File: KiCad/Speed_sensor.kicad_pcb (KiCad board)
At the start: 4 copper layers, 35 x 20 mm, 65 parts, among them J1 USB_B_Micro, J2 SWD, U1 BQ24040DSQR, U2 TP1941U, U3 ST1PS02, U4 nRF52832-QFxx, U5 LIS2DH12, Y1 32,768kHz, Y2 32MHz

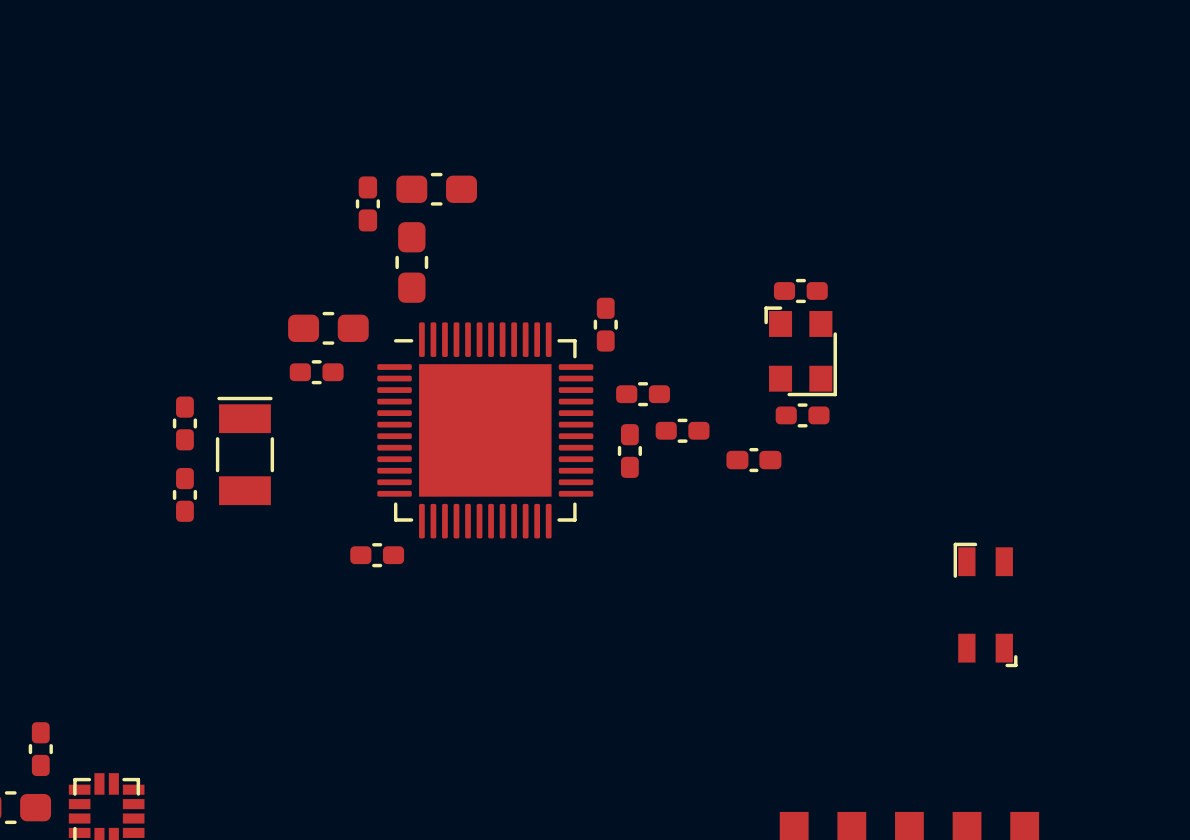
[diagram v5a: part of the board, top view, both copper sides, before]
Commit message: Layout um den nrf an Referenzlayout orientiert.
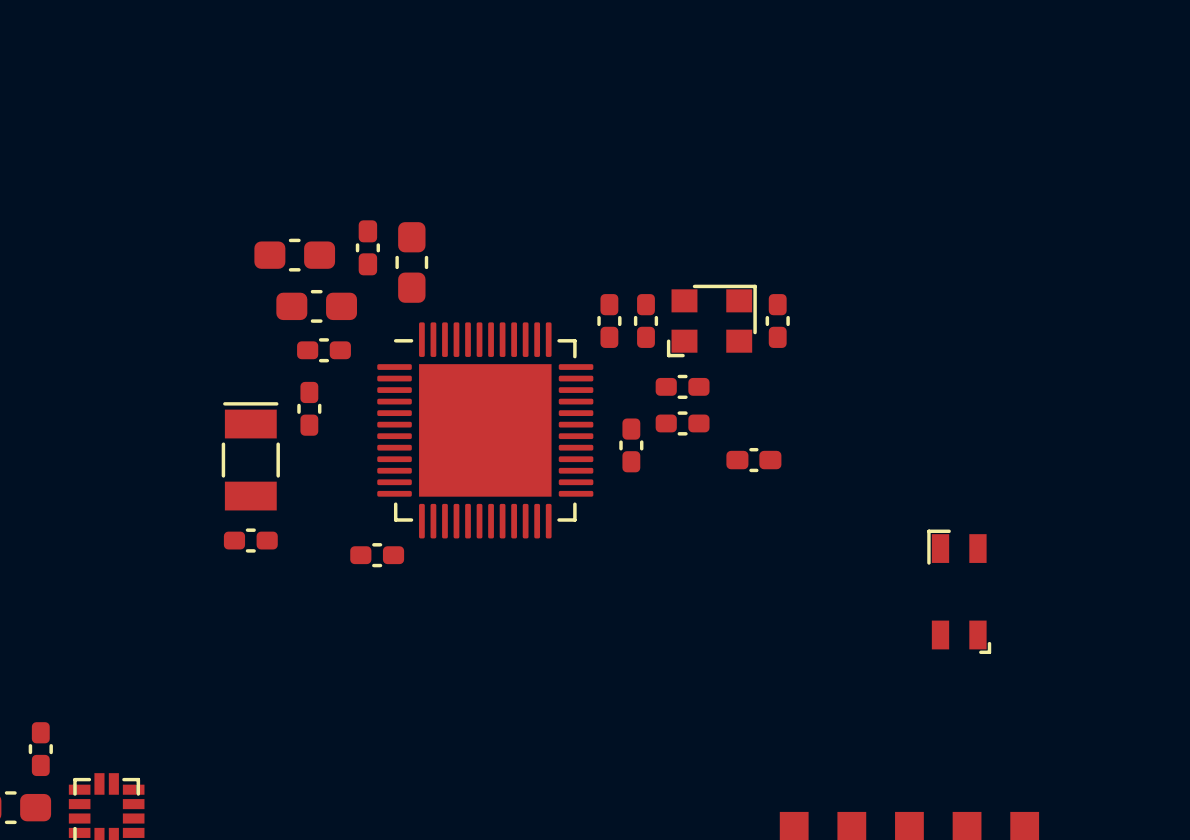
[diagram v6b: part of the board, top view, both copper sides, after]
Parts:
- moved C19 5.48 mm to (121.9, 50.8), turned to 90 degrees
- moved C14 5.43 mm to (109.7, 48.5), turned to 180 degrees
- moved C15 4.35 mm to (110.2, 53.8), turned to 90 degrees
- moved C18 3.39 mm to (126.5, 50.8), turned to 270 degrees
- moved Y2 3.26 mm to (124.2, 50.8), turned to 180 degrees
- moved C16 2.78 mm to (108.2, 58.4), turned to 180 degrees
- moved L2 1.52 mm to (112.3, 48.3), turned to 270 degrees
- moved C11 1.39 mm to (123.2, 53.1)
- moved AE1 1.02 mm to (132.8, 60.2)
- moved C8 0.86 mm to (110.5, 50.3)
- moved C13 0.80 mm to (110.7, 51.8)
- moved Y1 0.28 mm to (108.2, 55.6)
- moved C12 0.25 mm to (123.2, 54.4)
- moved C17 0.20 mm to (121.4, 55.1)
- moved C10 0.18 mm to (120.7, 50.8)

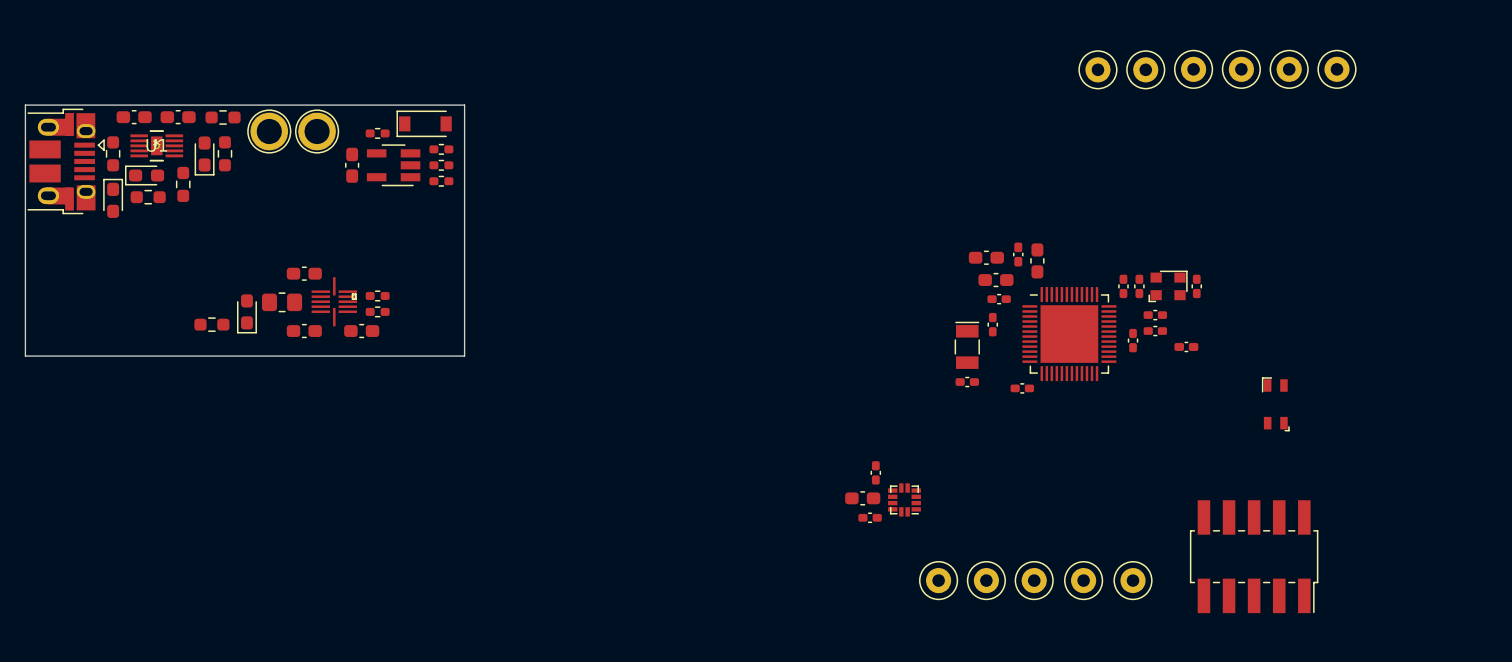
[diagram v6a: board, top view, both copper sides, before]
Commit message: kompletter power circuit kompakt im layout untergebracht.
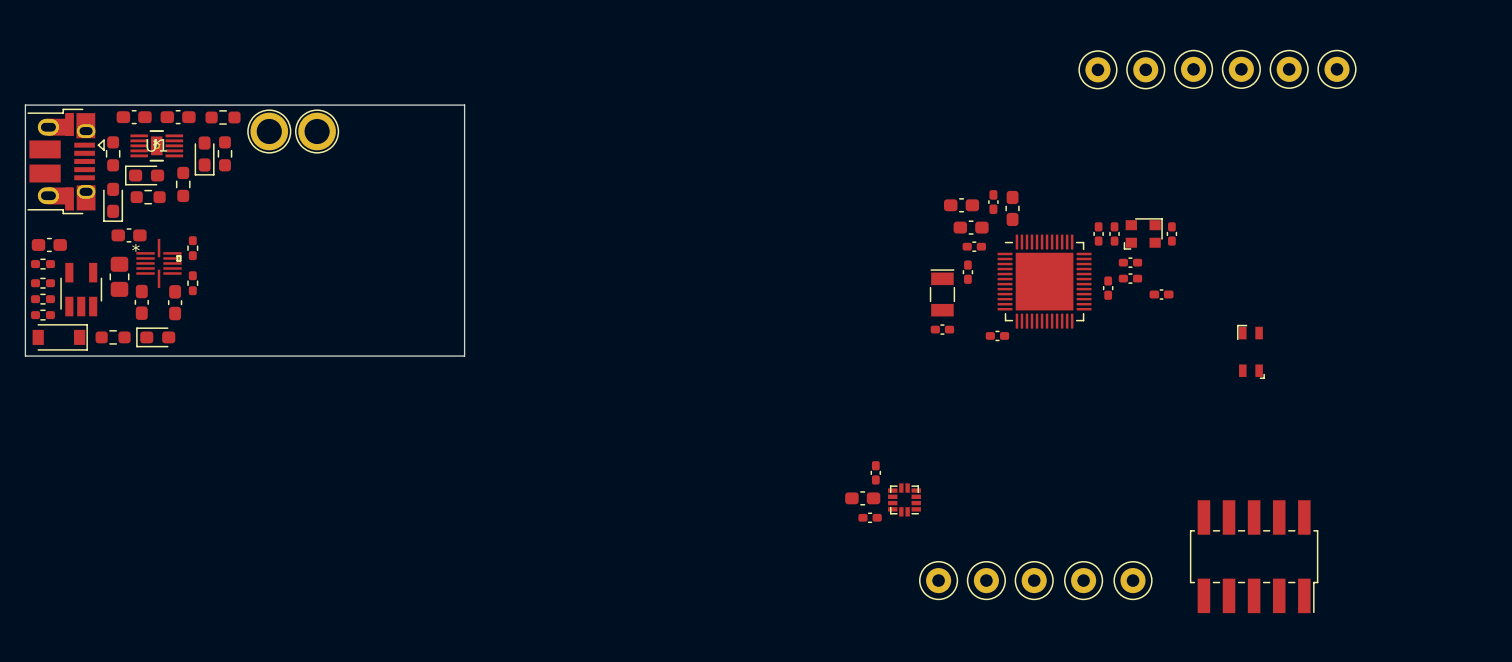
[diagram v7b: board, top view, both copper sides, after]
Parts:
- moved R6 34.4 mm to (34.5, 53.1), turned to 0 degrees
- moved D4 33.8 mm to (35.8, 54.9), turned to 180 degrees
- moved R7 33.5 mm to (34.5, 51.8), turned to 0 degrees
- moved R8 32.8 mm to (34.5, 50.5), turned to 180 degrees
- moved R9 28.6 mm to (34.5, 49.0), turned to 180 degrees
- moved U2 26.8 mm to (37.6, 51.1), turned to 90 degrees
- moved C3 25.0 mm to (35.1, 47.5), turned to 180 degrees
- moved R10 15.2 mm to (46.5, 47.8), turned to 90 degrees
- moved C6 15.0 mm to (45.1, 52.1), turned to 270 degrees
- moved R12 14.9 mm to (46.5, 50.5), turned to 270 degrees
- moved C4 14.3 mm to (41.4, 46.7)
- moved U3 14.3 mm to (43.8, 49.0)
- moved C7 13.2 mm to (42.4, 52.1), turned to 270 degrees
- moved L1 13.1 mm to (40.6, 50.0), turned to 270 degrees
- moved R11 7.94 mm to (40.1, 54.9)
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
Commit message: Bauteilplatzierungen leicht angepasst. Bemerkt, dass PCB wahrsch größer werden muss.
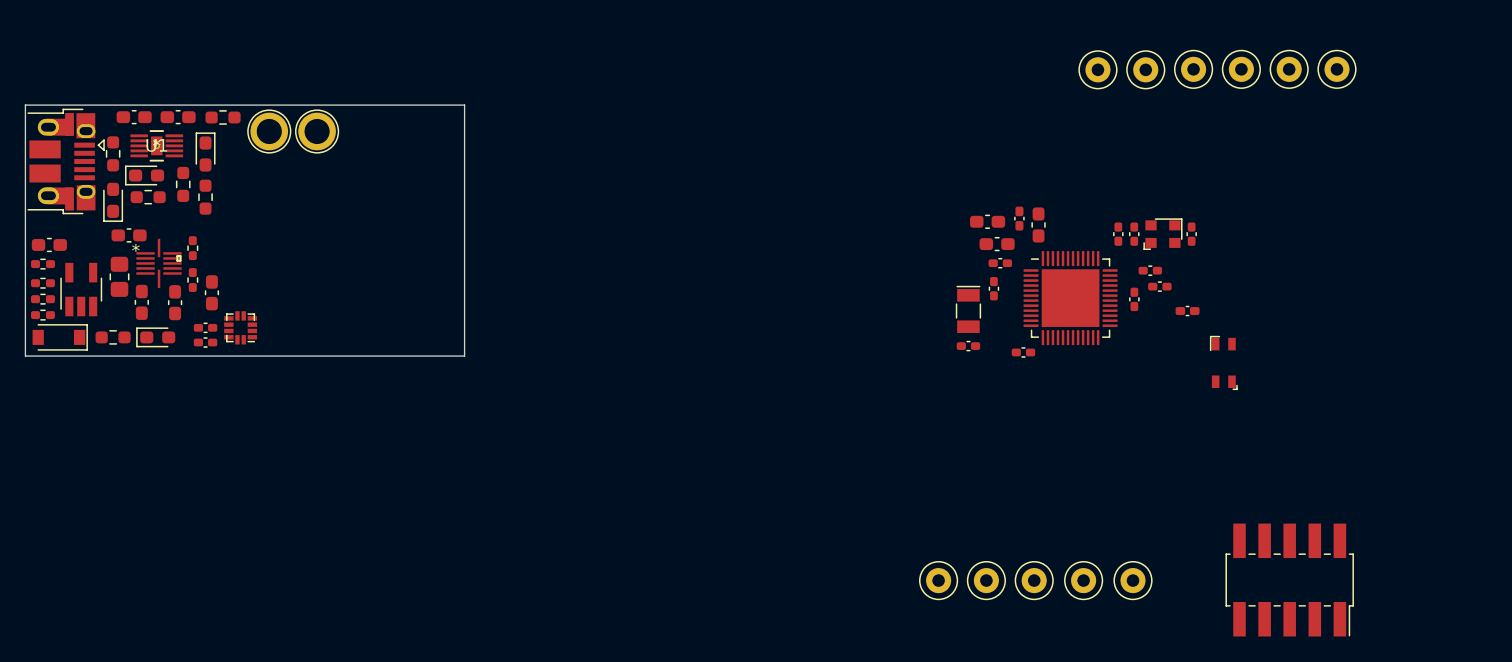
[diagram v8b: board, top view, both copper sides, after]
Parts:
- moved C5 54.8 mm to (47.5, 55.3)
- moved U5 54.7 mm to (50.3, 54.1)
- moved C20 54.7 mm to (47.5, 54.1), turned to 180 degrees
- moved C21 54.4 mm to (48.0, 51.3), turned to 90 degrees
- moved R5 3.79 mm to (47.5, 43.7)
- moved J2 3.39 mm to (133.9, 74.2)
- moved C15 2.45 mm to (110.3, 51.0)
- moved C9 2.45 mm to (112.7, 56.1)
- moved L2 2.45 mm to (112.4, 45.4)
- moved L3 2.45 mm to (113.9, 45.9)
- moved U4 2.45 mm to (116.4, 51.7)
- moved Y1 2.45 mm to (108.3, 52.8)
- moved C13 2.45 mm to (110.8, 49.0)
- moved C16 2.45 mm to (108.3, 55.6)
- moved L4 2.45 mm to (125.8, 52.8)
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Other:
- rule trace_min: 0.2 -> 0.09
- rule via_min_drill: 0.3 -> 0.2
